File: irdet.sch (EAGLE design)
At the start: 66 parts, among them IC1 MEGA8-AI, IC2 78L05F, J1 PSH02-04WG, J2 PSH02-04WG, J3 PSH02-04WG, J4 PSH02-04WG, J5 22-05-7098-09, T1 BC847, T2 BC857, T3 BC847, T4 BC857, T5 BC847, T6 BC857, T7 BC847, T8 BC857, X1 MVE252-5-V, X2 MVE252-5-V

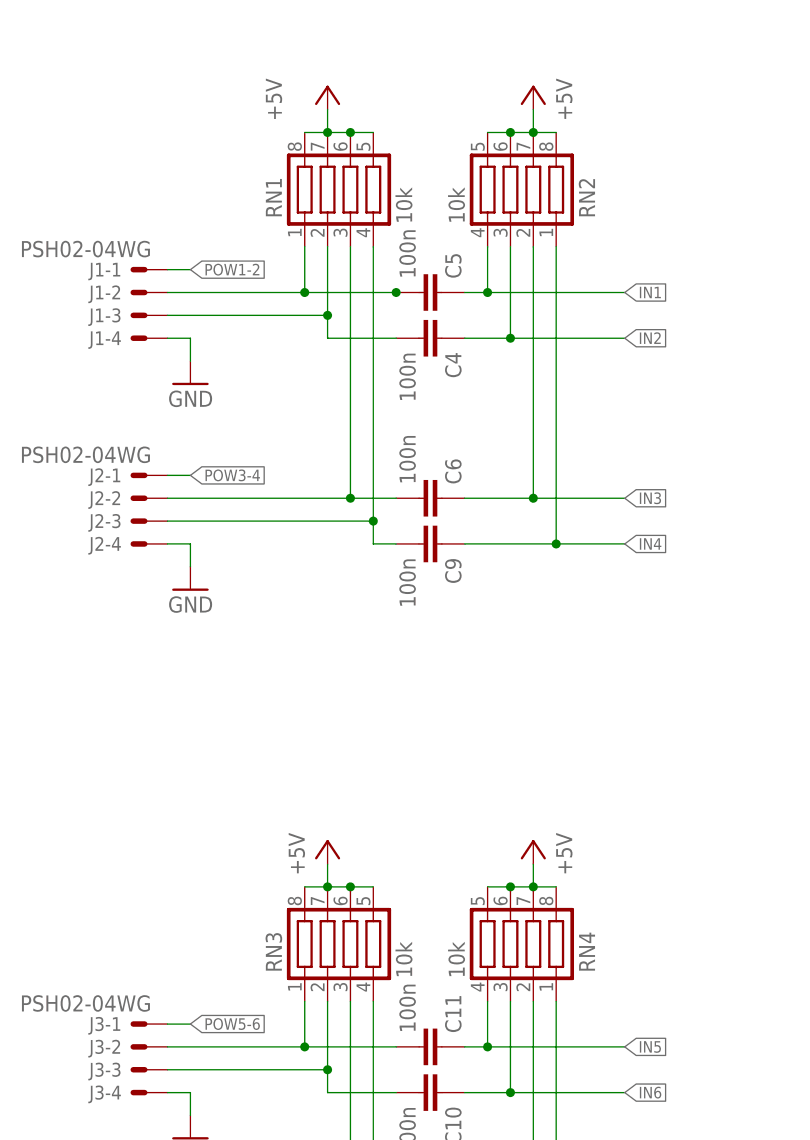
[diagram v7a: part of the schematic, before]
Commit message: Change pull-up input resistors to 100k.
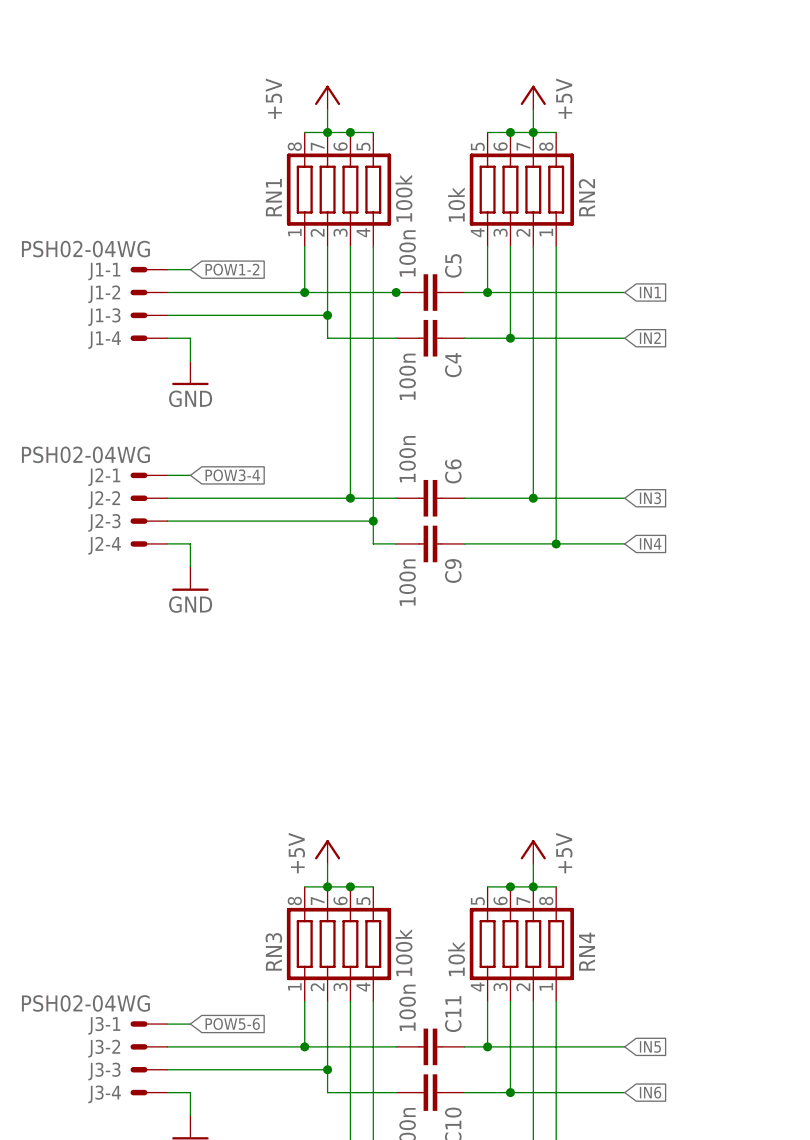
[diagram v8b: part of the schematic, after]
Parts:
- RN1, RN3: value 10k -> 100k; LCSC_PART C29718 -> C173315
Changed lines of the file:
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@@
 </part>
 <part name="GND3" library="supply1" library_urn="urn:adsk.eagle:library:371" deviceset="GND" device=""/>
-<part name="RN1" library="resistor-net" library_urn="urn:adsk.eagle:library:343" deviceset="CTS742C083" device="" package3d_urn="urn:adsk.eagle:package:24985/1" value="10k">
-<attribute name="LCSC_PART" value="C29718"/>
+<part name="RN1" library="resistor-net" library_urn="urn:adsk.eagle:library:343" deviceset="CTS742C083" device="" package3d_urn="urn:adsk.eagle:package:24985/1" value="100k">
+<attribute name="LCSC_PART" value="C173315"/>
 </part>
 <part name="C4" library="rcl" deviceset="C-EU" device="C0805" value="100n">
@@
 <part name="J3" library="con-molex" library_urn="urn:adsk.eagle:library:165" deviceset="22-?-04" device="05-7048" package3d_urn="urn:adsk.eagle:package:8078648/1" value="PSH02-04WG"/>
 <part name="GND5" library="supply1" library_urn="urn:adsk.eagle:library:371" deviceset="GND" device=""/>
-<part name="RN3" library="resistor-net" library_urn="urn:adsk.eagle:library:343" deviceset="CTS742C083" device="" package3d_urn="urn:adsk.eagle:package:24985/1" value="10k">
-<attribute name="LCSC_PART" value="C29718"/>
+<part name="RN3" library="resistor-net" library_urn="urn:adsk.eagle:library:343" deviceset="CTS742C083" device="" package3d_urn="urn:adsk.eagle:package:24985/1" value="100k">
+<attribute name="LCSC_PART" value="C173315"/>
 </part>
 <part name="C10" library="rcl" deviceset="C-EU" device="C0805" value="100n">
